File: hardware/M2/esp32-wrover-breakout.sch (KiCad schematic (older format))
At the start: 10 parts, among them IC1 ESP32-WROVER-E_M213EH6464PH3Q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, J1 Conn_01x06_Male, J2 Conn_01x10_Male, J3 Conn_01x10_Male, Q1 MUN5214DW1T1G, U1 XC6220B331MR

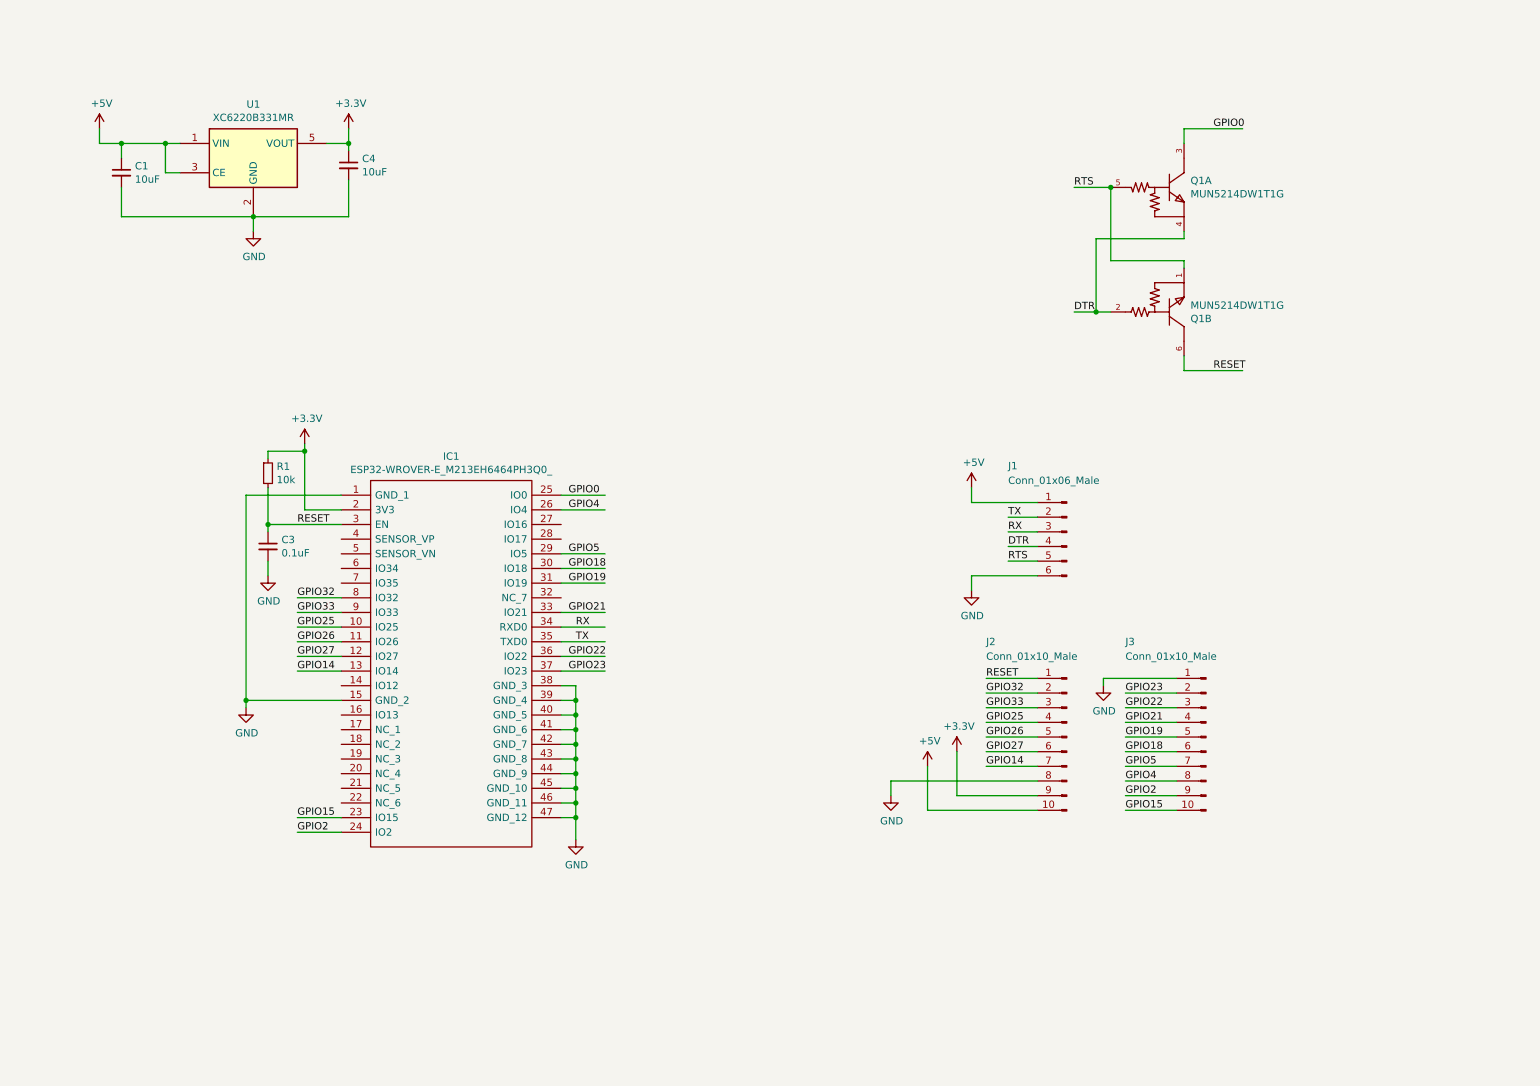
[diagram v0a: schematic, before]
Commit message: M.2 schematic + first placement
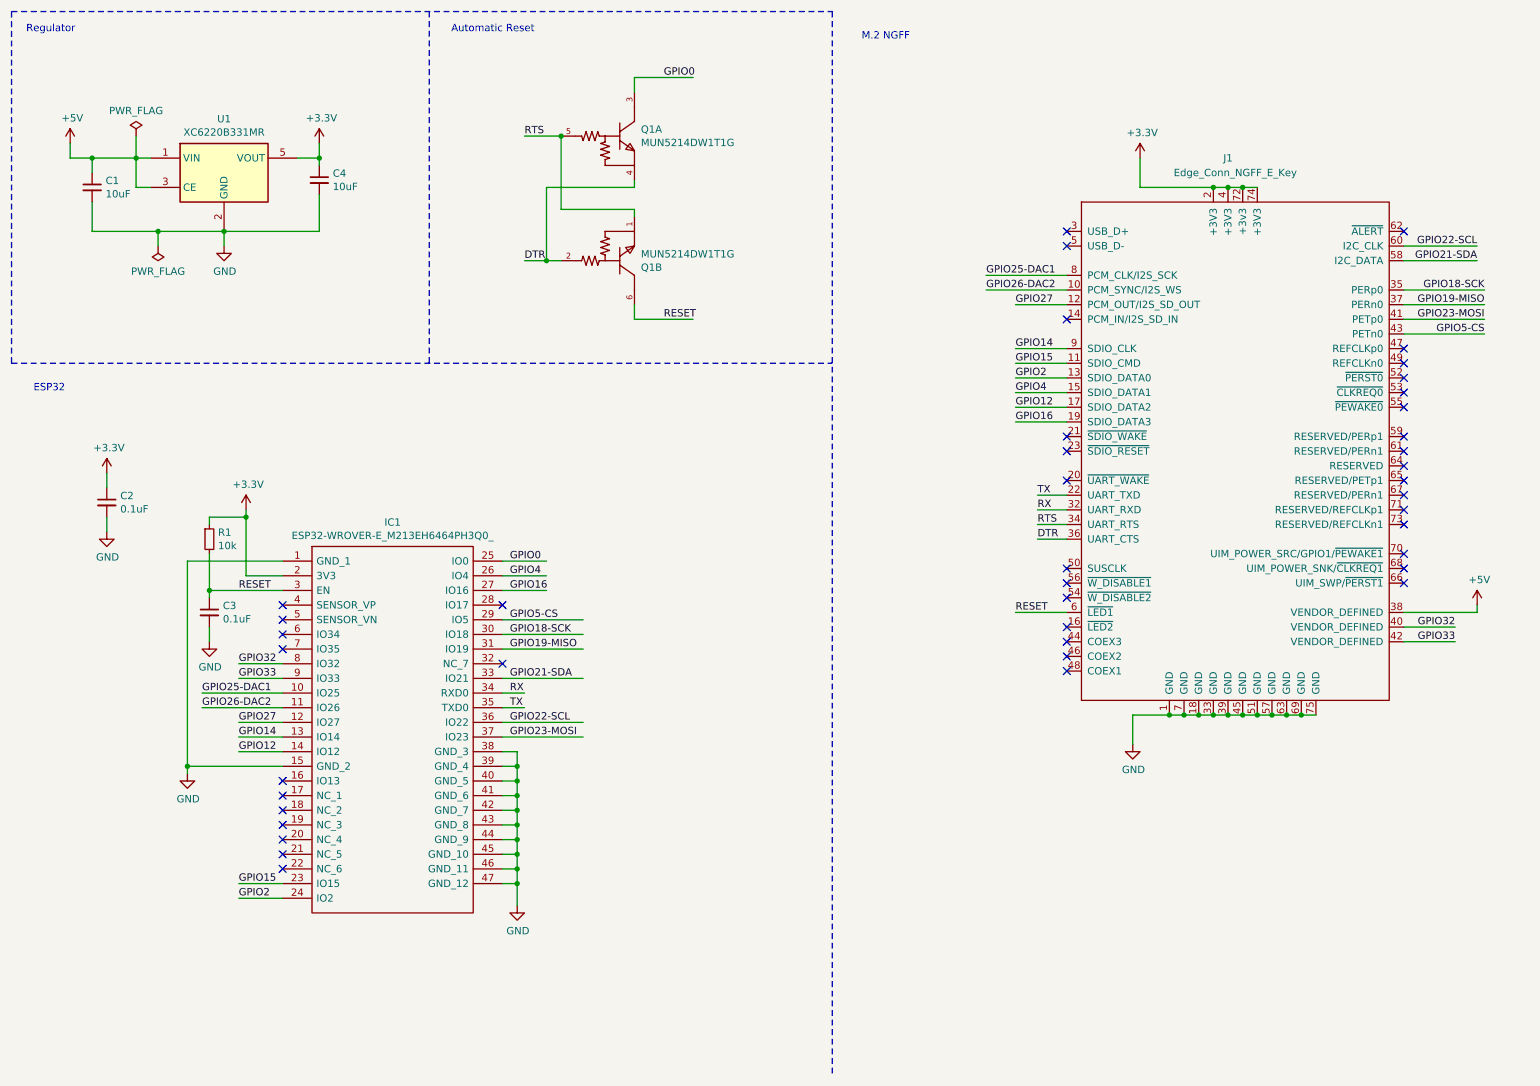
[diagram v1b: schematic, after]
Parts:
- removed J1: Conn_01x06_Male, B6B-ZR(LF)(SN):JST_B6B-ZR(LF)(SN), symbol Connector:Conn_01x06_Male
- removed J2, J3: Conn_01x10_Male, Connector_PinHeader_2.54mm:PinHeader_1x10_P2.54mm_Vertical, symbol Connector:Conn_01x10_Male
- added C2: 0.1uF, Capacitor_SMD:C_0603_1608Metric_Pad1.08x0.95mm_HandSolder, symbol Device:C_Small
- added J1: Edge_Conn_NGFF_E_Key, NGFF:NGFF_E, symbol M2:Edge_Conn_NGFF_E_Key
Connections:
- net labels added: GPIO12, GPIO16, GPIO18-SCK, GPIO19-MISO, GPIO21-SDA, GPIO22-SCL, GPIO23-MOSI, GPIO25-DAC1, GPIO26-DAC2, GPIO5-CS
- net labels removed: GPIO18, GPIO19, GPIO21, GPIO22, GPIO23, GPIO25, GPIO26, GPIO5
- wire segments 111 -> 127
- no-connect marks 0 -> 42
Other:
- note added: "Automatic Reset"
- note added: "ESP32"
- note added: "M.2 NGFF"
- note added: "Regulator"
- moved on the sheet: C1, C3, C4, IC1, Q1A, Q1B, R1, U1

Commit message: First M.2 routing
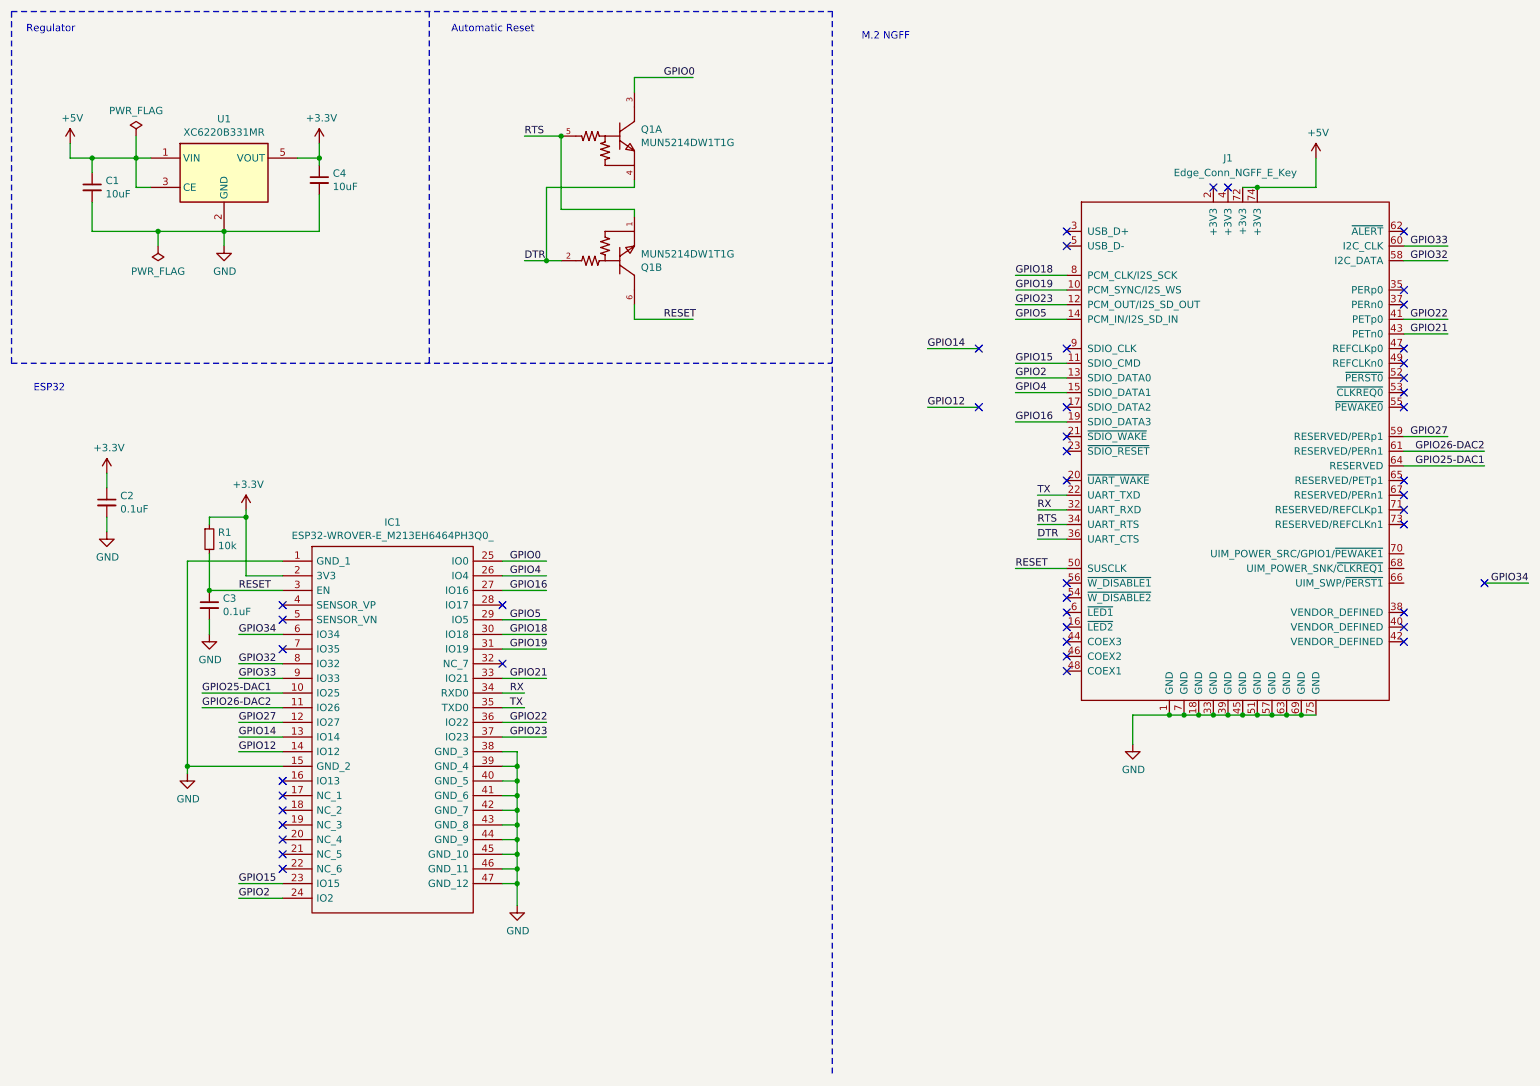
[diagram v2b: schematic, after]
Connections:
- net labels added: GPIO18, GPIO19, GPIO21, GPIO22, GPIO23, GPIO34, GPIO5
- net labels removed: GPIO18-SCK, GPIO19-MISO, GPIO21-SDA, GPIO22-SCL, GPIO23-MOSI, GPIO5-CS
- wire segments 127 -> 124
- no-connect marks 42 -> 46
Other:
- moved on the sheet: C3
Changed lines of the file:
@@
 L Device:C_Small C3
 U 1 1 5FF3A196
-P 1850 4600
-F 0 "C3" H 1942 4646 50  0000 L CNN
-F 1 "0.1uF" H 1942 4555 50  0000 L CNN
-F 2 "Capacitor_SMD:C_0603_1608Metric_Pad1.08x0.95mm_HandSolder" H 1850 4600 50  0001 C CNN
-F 3 "~" H 1850 4600 50  0001 C CNN
-	1    1850 4600
+P 1850 4550
+F 0 "C3" H 1942 4596 50  0000 L CNN
+F 1 "0.1uF" H 1942 4505 50  0000 L CNN
+F 2 "Capacitor_SMD:C_0603_1608Metric_Pad1.08x0.95mm_HandSolder" H 1850 4550 50  0001 C CNN
+F 3 "~" H 1850 4550 50  0001 C CNN
+	1    1850 4550
 	1    0    0    -1
 $EndComp
 Wire Wire Line
 	2350 4450 1850 4450
-Wire Wire Line
-	1850 4450 1850 4500
 $Comp
 L power:GND #PWR0102
 U 1 1 5FF40A52
-P 1850 4800
-F 0 "#PWR0102" H 1850 4550 50  0001 C CNN
-F 1 "GND" H 1855 4627 50  0000 C CNN
-F 2 "" H 1850 4800 50  0001 C CNN
-F 3 "" H 1850 4800 50  0001 C CNN
-	1    1850 4800
-	1    0    0    -1
-$EndComp
-Wire Wire Line
-	1850 4700 1850 4800
+P 1850 4750
+F 0 "#PWR0102" H 1850 4500 50  0001 C CNN
+F 1 "GND" H 1855 4577 50  0000 C CNN
+F 2 "" H 1850 4750 50  0001 C CNN
+F 3 "" H 1850 4750 50  0001 C CNN
+	1    1850 4750
+	1    0    0    -1
+$EndComp
+Wire Wire Line
+	1850 4650 1850 4750
 Text Label 2050 4450 0    50   ~ 0
 RESET
@@
 Wire Wire Line
 	3850 4250 4150 4250
-Text Label 7150 2400 0    50   ~ 0
+Text Label 10550 3500 2    50   ~ 0
 GPIO26-DAC2
-Text Label 7350 2500 0    50   ~ 0
+Text Label 10300 3400 2    50   ~ 0
 GPIO27
-Text Label 7350 2800 0    50   ~ 0
+Text Label 6750 2800 0    50   ~ 0
 GPIO14
 Wire Wire Line
@@
 Text Label 7350 3000 0    50   ~ 0
 GPIO2
-Text Label 10500 2200 2    50   ~ 0
-GPIO21-SDA
-Text Label 10550 2700 2    50   ~ 0
-GPIO5-CS
-Text Label 10550 2400 2    50   ~ 0
-GPIO18-SCK
-Text Label 10550 2600 2    50   ~ 0
-GPIO23-MOSI
+Text Label 10300 2700 2    50   ~ 0
+GPIO21
+Text Label 7350 2600 0    50   ~ 0
+GPIO5
+Text Label 7350 2300 0    50   ~ 0
+GPIO18
 Text Label 3900 5350 0    50   ~ 0
-GPIO22-SCL
+GPIO22
 Text Label 3900 5050 0    50   ~ 0
-GPIO21-SDA
+GPIO21
 $Comp
 L power:GND #PWR0106
@@
 Wire Wire Line
 	1850 4450 1850 4200
-Connection ~ 1850 4450
 Wire Wire Line
 	1850 4000 1850 3950
@@
 	2100 3950 2100 3900
 Connection ~ 2100 3950
-Wire Wire Line
-	8200 1700 8200 1500
 Text Label 7500 4000 0    50   ~ 0
 RTS
 Wire Wire Line
-	10500 2100 10000 2100
-Wire Wire Line
-	10550 2700 10000 2700
-Wire Wire Line
-	7150 2400 7700 2400
-Text Label 10550 2500 2    50   ~ 0
-GPIO19-MISO
+	10550 3500 10000 3500
 Text Label 7350 2900 0    50   ~ 0
 GPIO15
 Text Label 7350 3100 0    50   ~ 0
 GPIO4
-Text Label 7150 2300 0    50   ~ 0
+Text Label 10550 3600 2    50   ~ 0
 GPIO25-DAC1
 Text Label 2050 5550 0    50   ~ 0
@@
 Wire Wire Line
 	2350 5550 2050 5550
-Text Label 7350 3200 0    50   ~ 0
+Text Label 6750 3200 0    50   ~ 0
 GPIO12
 Wire Wire Line
@@
 Text Label 3900 4450 0    50   ~ 0
 GPIO16
-Text Label 7350 3300 0    50   ~ 0
-GPIO16
-Wire Wire Line
-	7350 3300 7700 3300
-Text Label 7350 4600 0    50   ~ 0
+Text Label 7350 4300 0    50   ~ 0
 RESET
 Wire Wire Line
-	7350 2500 7700 2500
-Wire Wire Line
-	7350 4600 7700 4600
+	7350 4300 7700 4300
 Wire Wire Line
 	7700 4000 7500 4000
@@
 	7700 4100 7500 4100
 Wire Wire Line
-	10500 2200 10000 2200
-Wire Wire Line
-	10550 2500 10000 2500
-Wire Wire Line
-	10550 2600 10000 2600
-Wire Wire Line
-	10550 2400 10000 2400
-Wire Wire Line
 	7700 3800 7500 3800
 Wire Wire Line
-	7350 3200 7700 3200
+	6750 3200 7100 3200
 Wire Wire Line
 	7350 3100 7700 3100
@@
 	7700 2900 7350 2900
 Wire Wire Line
-	7150 2300 7700 2300
-$Comp
-L M2:Edge_Conn_NGFF_E_Key J1
-U 1 1 5FFE778E
-P 8700 5400
-F 0 "J1" H 8800 9300 50  0000 C CNN
-F 1 "Edge_Conn_NGFF_E_Key" H 8850 9200 50  0000 C CNN
-F 2 "NGFF:NGFF_E" H 8700 5400 50  0001 C CNN
-F 3 "" H 8700 5400 50  0001 C CNN
-	1    8700 5400
-	1    0    0    -1
-$EndComp
+	10550 3600 10000 3600
 $Comp
 L power:GND #PWR0110
@@
 	1    0    0    -1
 $EndComp
-Wire Wire Line
-	8200 1700 8700 1700
-Text Label 10500 2100 2    50   ~ 0
-GPIO22-SCL
-Connection ~ 8700 1700
-Wire Wire Line
-	8700 1700 8800 1700
-Connection ~ 8800 1700
-Wire Wire Line
-	8800 1700 8900 1700
-Connection ~ 8900 1700
-Wire Wire Line
-	8900 1700 9000 1700
-Wire Wire Line
-	9400 5300 9300 5300
+Text Label 10300 2600 2    50   ~ 0
+GPIO22
 Wire Wire Line
 	8150 5300 8150 5500
-Connection ~ 8400 5300
-Wire Wire Line
-	8400 5300 8150 5300
-Connection ~ 8500 5300
-Wire Wire Line
-	8500 5300 8400 5300
-Connection ~ 8600 5300
-Wire Wire Line
-	8600 5300 8500 5300
-Connection ~ 8700 5300
-Wire Wire Line
-	8700 5300 8600 5300
-Connection ~ 8800 5300
-Wire Wire Line
-	8800 5300 8700 5300
-Connection ~ 8900 5300
-Wire Wire Line
-	8900 5300 8800 5300
-Connection ~ 9000 5300
-Wire Wire Line
-	9000 5300 8900 5300
-Connection ~ 9100 5300
-Wire Wire Line
-	9100 5300 9000 5300
-Connection ~ 9200 5300
-Wire Wire Line
-	9200 5300 9100 5300
-Connection ~ 9300 5300
-Wire Wire Line
-	9300 5300 9200 5300
 Text Notes 3500 650  0    50   ~ 0
 Automatic Reset
@@
 Regulator
 Wire Wire Line
-	7700 2800 7350 2800
+	7100 2800 6750 2800
 Text Label 1800 5150 0    50   ~ 0
 GPIO25-DAC1
@@
 Wire Wire Line
 	1800 5250 2350 5250
-Wire Wire Line
-	3850 5050 4400 5050
-Wire Wire Line
-	3850 5350 4400 5350
 Text Label 3900 4750 0    50   ~ 0
-GPIO18-SCK
+GPIO18
 Text Label 3900 4850 0    50   ~ 0
-GPIO19-MISO
+GPIO19
 Text Label 3900 5450 0    50   ~ 0
-GPIO23-MOSI
+GPIO23
 Wire Wire Line
 	3850 5150 4000 5150
 Wire Wire Line
 	3850 5250 4000 5250
-Wire Wire Line
-	3850 5450 4400 5450
-Wire Wire Line
-	3850 4850 4400 4850
-Wire Wire Line
-	3850 4750 4400 4750
 Text Label 3900 4650 0    50   ~ 0
-GPIO5-CS
-Wire Wire Line
-	3850 4650 4400 4650
+GPIO5
 NoConn ~ 3850 4550
 NoConn ~ 3850 4950
 NoConn ~ 2350 4550
 NoConn ~ 2350 4650
-NoConn ~ 2350 4750
 NoConn ~ 2350 4850
 NoConn ~ 2350 5750
@@
 NoConn ~ 7700 2000
 NoConn ~ 7700 2100
-NoConn ~ 7700 2600
+NoConn ~ 10000 3700
 NoConn ~ 7700 3400
 NoConn ~ 7700 3500
 NoConn ~ 7700 3700
-NoConn ~ 7700 4300
+NoConn ~ 7700 4600
 NoConn ~ 7700 4400
 NoConn ~ 7700 4500
@@
 NoConn ~ 10000 3100
 NoConn ~ 10000 3200
-NoConn ~ 10000 3400
-NoConn ~ 10000 3500
-NoConn ~ 10000 3600
-NoConn ~ 10000 3700
+NoConn ~ 10000 2500
+NoConn ~ 10000 2400
 NoConn ~ 10000 3800
 NoConn ~ 10000 3900
 NoConn ~ 10000 4000
-NoConn ~ 10000 4200
-NoConn ~ 10000 4300
-NoConn ~ 10000 4400
+NoConn ~ 10000 4600
+NoConn ~ 10000 4700
+NoConn ~ 10000 4800
 $Comp
 L power:PWR_FLAG #FLG0101
@@
 Wire Wire Line
 	1150 3650 1150 3750
-$Comp
-L power:+3.3V #PWR0109
-U 1 1 60059D17
-P 8200 1500
-F 0 "#PWR0109" H 8200 1350 50  0001 C CNN
-F 1 "+3.3V" H 8215 1673 50  0000 C CNN
-F 2 "" H 8200 1500 50  0001 C CNN
-F 3 "" H 8200 1500 50  0001 C CNN
-	1    8200 1500
-	1    0    0    -1
-$EndComp
-Text Label 10350 4700 2    50   ~ 0
+Text Label 10300 2200 2    50   ~ 0
 GPIO32
-Text Label 10350 4800 2    50   ~ 0
+Text Label 10300 2100 2    50   ~ 0
 GPIO33
 Wire Wire Line
-	10350 4800 10000 4800
-Wire Wire Line
-	10350 4700 10000 4700
+	1150 3950 1150 4050
+Wire Wire Line
+	2350 4750 2050 4750
+Text Label 2050 4750 0    50   ~ 0
+GPIO34
+Connection ~ 1850 4450
+Text Label 10850 4400 2    50   ~ 0
+GPIO34
+Text Label 7350 2400 0    50   ~ 0
+GPIO19
+Text Label 7350 2500 0    50   ~ 0
+GPIO23
+Wire Wire Line
+	10000 3400 10300 3400
+Wire Wire Line
+	10000 2200 10300 2200
+Wire Wire Line
+	10300 2100 10000 2100
+Wire Wire Line
+	10550 4400 10850 4400
+NoConn ~ 10550 4400
+Wire Wire Line
+	3850 5050 4150 5050
+Wire Wire Line
+	4150 5350 3850 5350
+Wire Wire Line
+	10000 2600 10300 2600
+Wire Wire Line
+	10000 2700 10300 2700
+NoConn ~ 7700 2800
+NoConn ~ 7100 2800
+NoConn ~ 7100 3200
+NoConn ~ 7700 3200
+Wire Wire Line
+	3850 4650 4150 4650
+Wire Wire Line
+	3850 4750 4150 4750
+Wire Wire Line
+	4150 4850 3850 4850
+Wire Wire Line
+	4150 5450 3850 5450
+Wire Wire Line
+	7700 2300 7350 2300
+Wire Wire Line
+	7350 2400 7700 2400
+Wire Wire Line
+	7700 2500 7350 2500
+Wire Wire Line
+	7350 2600 7700 2600
+Wire Wire Line
+	7350 3300 7700 3300
+Text Label 7350 3300 0    50   ~ 0
+GPIO16
+NoConn ~ 8700 1700
+NoConn ~ 8800 1700
+Connection ~ 9300 5300
+Wire Wire Line
+	9200 5300 9100 5300
+Connection ~ 9200 5300
+Connection ~ 9100 5300
+Wire Wire Line
+	9100 5300 9000 5300
+Wire Wire Line
+	9000 5300 8900 5300
+Connection ~ 9000 5300
+Connection ~ 8900 5300
+Wire Wire Line
+	8900 5300 8800 5300
+Wire Wire Line
+	8800 5300 8700 5300
+Connection ~ 8800 5300
+Connection ~ 8700 5300
+Wire Wire Line
+	8700 5300 8600 5300
+Wire Wire Line
+	8600 5300 8500 5300
+Connection ~ 8600 5300
+Connection ~ 8500 5300
+Wire Wire Line
+	8500 5300 8400 5300
+Wire Wire Line
+	8400 5300 8150 5300
+Connection ~ 8400 5300
+Wire Wire Line
+	9300 5300 9200 5300
+Wire Wire Line
+	9400 5300 9300 5300
 $Comp
 L power:+5V #PWR0108
-U 1 1 603AA727
-P 10500 4550
-F 0 "#PWR0108" H 10500 4400 50  0001 C CNN
-F 1 "+5V" H 10515 4723 50  0000 C CNN
-F 2 "" H 10500 4550 50  0001 C CNN
-F 3 "" H 10500 4550 50  0001 C CNN
-	1    10500 4550
-	1    0    0    -1
-$EndComp
-Wire Wire Line
-	10500 4550 10500 4600
-Wire Wire Line
-	10500 4600 10000 4600
-Wire Wire Line
-	1150 3950 1150 4050
+U 1 1 606DE2F0
+P 9400 1500
+F 0 "#PWR0108" H 9400 1350 50  0001 C CNN
+F 1 "+5V" H 9415 1673 50  0000 C CNN
+F 2 "" H 9400 1500 50  0001 C CNN
+F 3 "" H 9400 1500 50  0001 C CNN
+	1    9400 1500
+	1    0    0    -1
+$EndComp
+$Comp
+L M2:Edge_Conn_NGFF_E_Key J1
+U 1 1 5FFE778E
+P 8700 5400
+F 0 "J1" H 8800 9300 50  0000 C CNN
+F 1 "Edge_Conn_NGFF_E_Key" H 8850 9200 50  0000 C CNN
+F 2 "NGFF:NGFF_E" H 8700 5400 50  0001 C CNN
+F 3 "" H 8700 5400 50  0001 C CNN
+	1    8700 5400
+	1    0    0    -1
+$EndComp
+Wire Wire Line
+	8900 1700 9000 1700
+Wire Wire Line
+	9400 1700 9400 1500
+Connection ~ 9000 1700
+Wire Wire Line
+	9000 1700 9400 1700
 $EndSCHEMATC
